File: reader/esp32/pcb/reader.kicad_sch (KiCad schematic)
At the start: 28 parts, among them J1 Conn_01x06, J2 Conn_01x02, J3 Conn_01x04, J4 Conn_01x02, Q1 MMBT3904, Q2 MMBT3904, U1 ESP32-WROOM-32U, U2 RF125-PS, U3 CH340C, U4 74LVC1T45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

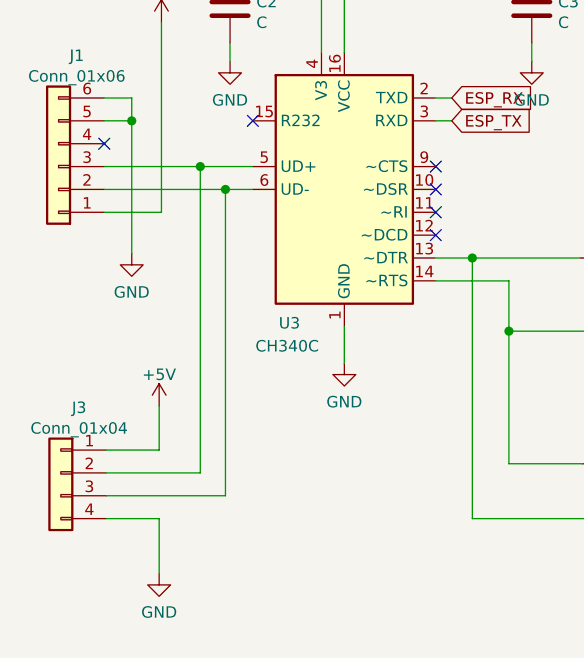
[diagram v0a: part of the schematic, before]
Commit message: Fix switched D-/D+.
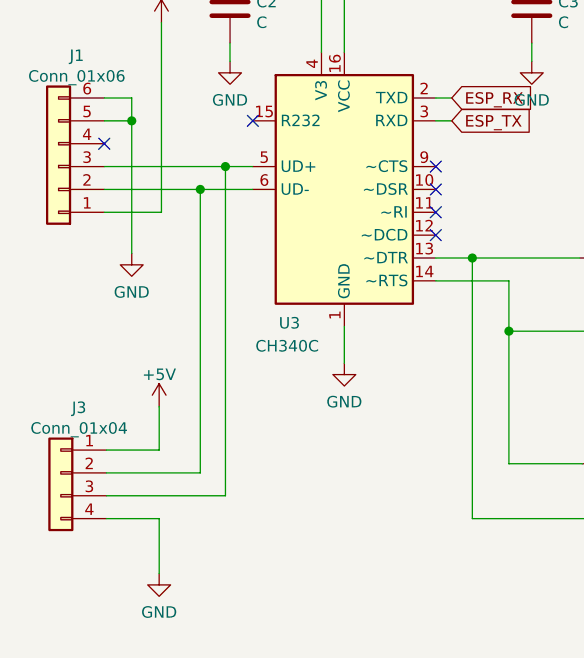
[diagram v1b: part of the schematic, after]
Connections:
- net at J1.2 (Pin_2), U3.6 (UD-): now also J3.2 (Pin_2); no longer J3.3 (Pin_3)
- net at J1.3 (Pin_3), U3.5 (UD+): now also J3.3 (Pin_3); no longer J3.2 (Pin_2)
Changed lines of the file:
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@@
   (paper "A4")
   (junction (at 32.258 58.42) (diameter 1.016) (color 0 0 0 0))
-  (junction (at 39.878 63.5) (diameter 1.016) (color 0 0 0 0))
-  (junction (at 42.672 66.04) (diameter 1.016) (color 0 0 0 0))
+  (junction (at 39.878 66.04) (diameter 1.016) (color 0 0 0 0))
+  (junction (at 42.672 63.5) (diameter 1.016) (color 0 0 0 0))
   (junction (at 43.434 146.812) (diameter 1.016) (color 0 0 0 0))
   (junction (at 43.434 156.464) (diameter 1.016) (color 0 0 0 0))
@@
     (stroke (width 0) (type solid) (color 0 0 0 0))
   )
-  (wire (pts (xy 29.21 63.5) (xy 39.878 63.5))
+  (wire (pts (xy 29.21 63.5) (xy 42.672 63.5))
     (stroke (width 0) (type solid) (color 0 0 0 0))
   )
-  (wire (pts (xy 29.21 66.04) (xy 42.672 66.04))
+  (wire (pts (xy 29.21 66.04) (xy 39.878 66.04))
     (stroke (width 0) (type solid) (color 0 0 0 0))
   )
@@
     (stroke (width 0) (type solid) (color 0 0 0 0))
   )
-  (wire (pts (xy 39.878 63.5) (xy 45.72 63.5))
+  (wire (pts (xy 39.878 66.04) (xy 39.878 97.536))
     (stroke (width 0) (type solid) (color 0 0 0 0))
   )
-  (wire (pts (xy 39.878 97.536) (xy 39.878 63.5))
+  (wire (pts (xy 39.878 66.04) (xy 45.72 66.04))
     (stroke (width 0) (type solid) (color 0 0 0 0))
   )
@@
     (stroke (width 0) (type solid) (color 0 0 0 0))
   )
-  (wire (pts (xy 42.672 66.04) (xy 45.72 66.04))
+  (wire (pts (xy 42.672 63.5) (xy 42.672 100.076))
     (stroke (width 0) (type solid) (color 0 0 0 0))
   )
-  (wire (pts (xy 42.672 100.076) (xy 42.672 66.04))
+  (wire (pts (xy 42.672 63.5) (xy 45.72 63.5))
     (stroke (width 0) (type solid) (color 0 0 0 0))
   )

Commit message: Fix 3D models.
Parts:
- J4: footprint Connector_PinHeader_2.54mm:PinHeader_1x02_P2.54mm_Vertical -> Connector_JST:JST_XH_S02B-XH-A-1_1x02_P2.50mm_Horizontal

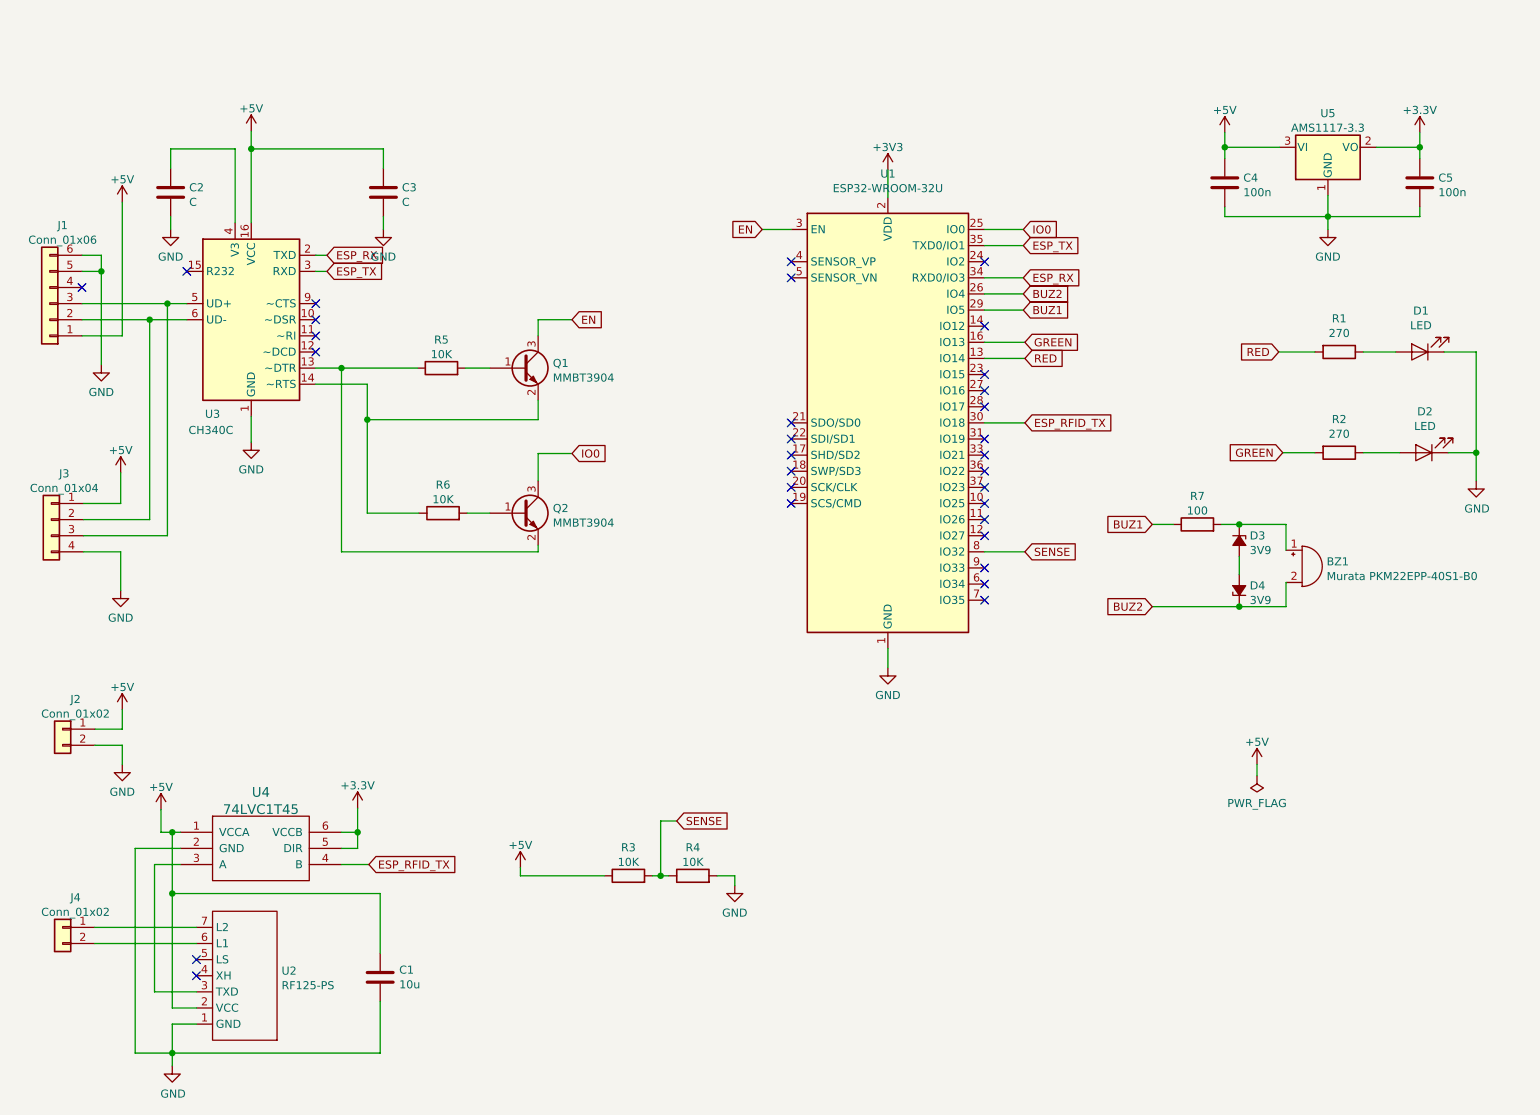
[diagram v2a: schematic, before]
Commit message: Retry reopen of serial port.
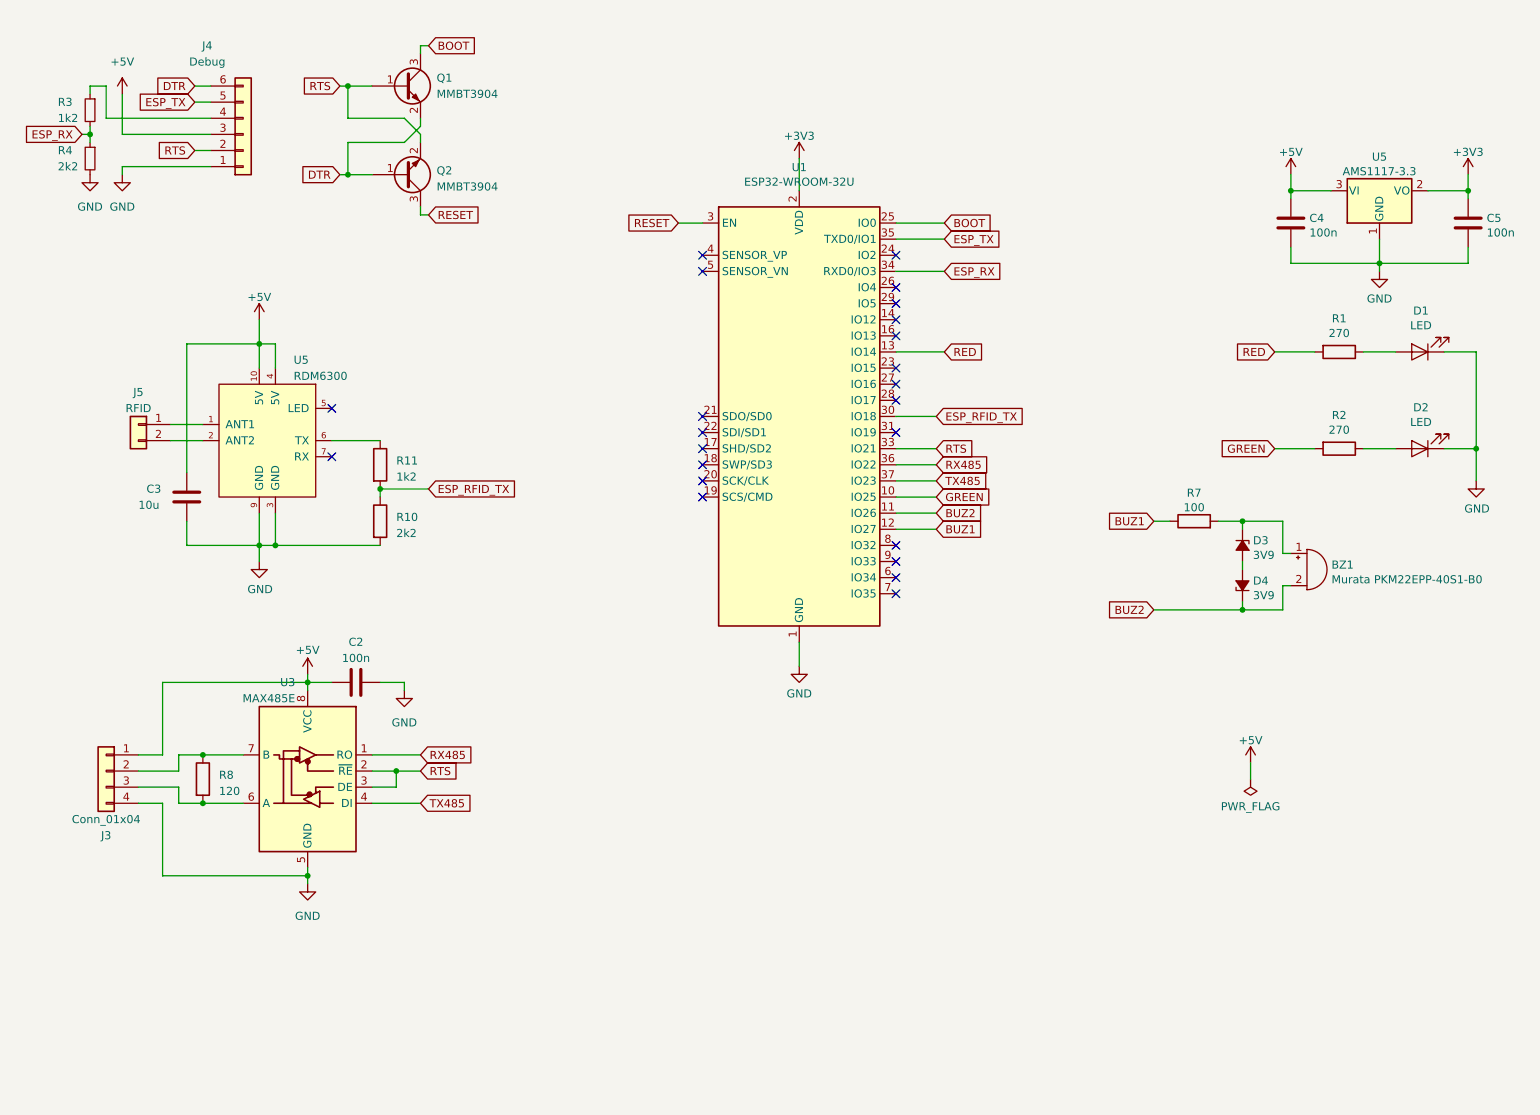
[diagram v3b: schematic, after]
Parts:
- removed C1: 10u, Capacitor_SMD:C_0805_2012Metric, symbol Device:C
- removed J1: Conn_01x06, Connector_USB:USB_Micro-B_Molex-105017-0001, symbol Connector_Generic:Conn_01x06
- removed J2, J4: Conn_01x02, Connector_JST:JST_XH_S02B-XH-A-1_1x02_P2.50mm_Horizontal, symbol Connector_Generic:Conn_01x02
- removed Q1, Q2: MMBT3904, Package_TO_SOT_SMD:SOT-23, symbol Device:Q_NPN_BEC
- removed R3, R4, R5, R6: 10K, Resistor_SMD:R_0603_1608Metric, symbol Device:R
- removed U2: RF125-PS, Module:rf125ps, symbol rf125ps:RF125-PS
- removed U3: CH340C, Package_SO:SOIC-16_3.9x9.9mm_P1.27mm, symbol Interface_USB:CH340C
- removed U4: 74LVC1T45, Package_TO_SOT_SMD:SOT-23-6, symbol 74lvc:74LVC1T45
- added J4: Debug, Connector_PinHeader_2.54mm:PinHeader_1x06_P2.54mm_Vertical, symbol Connector_Generic:Conn_01x06
- added J5: RFID, Connector_PinHeader_2.54mm:PinHeader_1x02_P2.54mm_Vertical, symbol Connector_Generic:Conn_01x02
- added Q1, Q2: MMBT3904, Package_TO_SOT_SMD:SOT-23, symbol Transistor_BJT:MMBT3904
- added R10: 2k2, Resistor_SMD:R_0603_1608Metric, symbol Device:R
- added R11: 1k2, Resistor_SMD:R_0603_1608Metric, symbol Device:R
- added R3: 1k2, Resistor_SMD:R_0603_1608Metric, symbol Device:R_Small
- added R4: 2k2, Resistor_SMD:R_0603_1608Metric, symbol Device:R_Small
- added R8: 120, Resistor_SMD:R_0603_1608Metric, symbol Device:R
- added U3: MAX485E, Housings_SOIC:SOIC-8_3.9x4.9mm_Pitch1.27mm, symbol Interface_UART:MAX485E
- added U5: RDM6300, Module:RDM6300_B38.5x18.2mm, symbol gtrzps:RDM6300
- C2: value C -> 100n
- C3: value C -> 10u
- J3: footprint Connector_JST:JST_PH_B4B-PH-K_1x04_P2.00mm_Vertical -> Connector_JST:JST_XH_S04B-XH-A_1x04_P2.50mm_Horizontal
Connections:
- net +5V: now also C2.1, J4.3 (Pin_3), U3.8 (VCC), U5.10 (5V), U5.4 (5V)
- net BUZ1: now also U1.12 (IO27); no longer U1.29 (IO5)
- net BUZ2: now also U1.11 (IO26); no longer U1.26 (IO4)
- net ESP_RFID_TX: now also R10.1, R11.2
- net ESP_RX: now also R3.2, R4.1
- net ESP_TX: now also J4.5 (Pin_5)
- net GND: now also J4.1 (Pin_1), R10.2, R4.2, U3.5 (GND), U5.3 (GND), U5.9 (GND)
- net GREEN: now also U1.10 (IO25); no longer U1.16 (IO13)
- net at J3.2 (Pin_2): now also R8.1, U3.7 (B)
- net at J3.3 (Pin_3): now also R8.2, U3.6 (A)
- net RTS: now reaches U1.33 (IO21)
- net RTS: now also J4.2 (Pin_2), Q1.1 (B), Q2.2 (E), U3.2 (~{RE}), U3.3 (DE)
- net RX485: now reaches U1.36 (IO22)
- net RX485: now also U3.1 (RO)
- net TX485: now reaches U1.37 (IO23)
- net TX485: now also U3.4 (DI)
- net EN renamed RESET
- net RESET: now also Q2.3 (C)
- net IO0 renamed BOOT
- net BOOT: now also Q1.3 (C)
- net SENSE: no longer names the net of U1.8 (IO32)
- new net: R11.1, U5.6 (TX)
- new net: J4.4 (Pin_4), R3.1
- new net: J5.1 (Pin_1), U5.1 (ANT1)
- new net: J5.2 (Pin_2), U5.2 (ANT2)
- new net DTR: J4.6 (Pin_6), Q1.2 (E), Q2.1 (B)
- no-connect marks 31 -> 23
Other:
- moved on the sheet: BZ1, C4, C5, D2, D3, D4, R2, R7, U1, U5

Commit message: USe RS-485 instead of USB.
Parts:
- removed J5: RFID, Connector_PinHeader_2.54mm:PinHeader_1x02_P2.54mm_Vertical, symbol Connector_Generic:Conn_01x02
- J2: renamed from J3; value Conn_01x04 -> RS485
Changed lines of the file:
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@@
-    (stroke (width 0) (type default))
-  )
-  (wire (pts (xy 43.18 85.09) (xy 48.26 85.09))
     (stroke (width 0) (type default))
   )
@@
   )
   (wire (pts (xy 212.09 110.49) (xy 212.09 111.76))
-    (stroke (width 0) (type default))
-  )
-  (wire (pts (xy 43.18 82.55) (xy 48.26 82.55))
     (stroke (width 0) (type default))
   )
@@
   (symbol (lib_id "Connector_Generic:Conn_01x04") (at 33.02 137.16 0) (mirror y) (unit 1)
     (in_bom yes) (on_board yes) (dnp no)
-    (property "Reference" "J3" (at 33.02 147.32 0)
-      (effects (font (size 1.27 1.27)))
-    )
-    (property "Value" "Conn_01x04" (at 33.02 144.78 0)
+    (property "Reference" "J2" (at 33.02 147.32 0)
+      (effects (font (size 1.27 1.27)))
+    )
+    (property "Value" "RS485" (at 33.02 144.78 0)
       (effects (font (size 1.27 1.27)))
     )
@@
       (project "reader"
         (path "/218f1b12-ca06-4253-bcd5-950f07f2eb16"
-          (reference "J3") (unit 1)
+          (reference "J2") (unit 1)
         )
       )
@@
     )
   )
-  (symbol (lib_id "Connector_Generic:Conn_01x02") (at 38.1 82.55 0) (mirror y) (unit 1)
-    (in_bom yes) (on_board yes) (dnp no) (fields_autoplaced)
-    (property "Reference" "J5" (at 38.1 77.47 0)
-      (effects (font (size 1.27 1.27)))
-    )
-    (property "Value" "RFID" (at 38.1 80.01 0)
-      (effects (font (size 1.27 1.27)))
-    )
-    (property "Footprint" "Connector_PinHeader_2.54mm:PinHeader_1x02_P2.54mm_Vertical" (at 38.1 82.55 0)
-      (effects (font (size 1.27 1.27)) hide)
-    )
-    (property "Datasheet" "~" (at 38.1 82.55 0)
-      (effects (font (size 1.27 1.27)) hide)
-    )
-    (pin "1")
-    (pin "2")
-    (instances
-      (project "bigbro_box"
-        (path "/212a0d71-cc7b-49f8-b4ca-a935e5355dca"
-          (reference "J5") (unit 1)
-        )
-      )
-      (project "reader"
-        (path "/218f1b12-ca06-4253-bcd5-950f07f2eb16"
-          (reference "J2") (unit 1)
-        )
-      )
-    )
-  )
   (symbol (lib_id "Device:R_Small") (at 30.48 40.64 0) (mirror y) (unit 1)
     (in_bom yes) (on_board yes) (dnp no)
@@
       (effects (font (size 1.27 1.27)) hide)
     )
-    (pin "1")
     (pin "10")
-    (pin "2")
     (pin "3")
     (pin "4")
